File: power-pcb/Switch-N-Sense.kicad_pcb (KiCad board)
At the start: 2 copper layers, 94 x 57.5 mm, 44 parts, among them P1 CONN_01X01, P2 CONN_01X01, P3 CONN_01X01, P4 CONN_01X01, P5 CONN_01X01, P6 Conn_Switch-N-Sense, Q1 CSD18540Q5B, Q2 CSD18540Q5B, Q3 CSD18540Q5B, Q4 CSD18540Q5B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

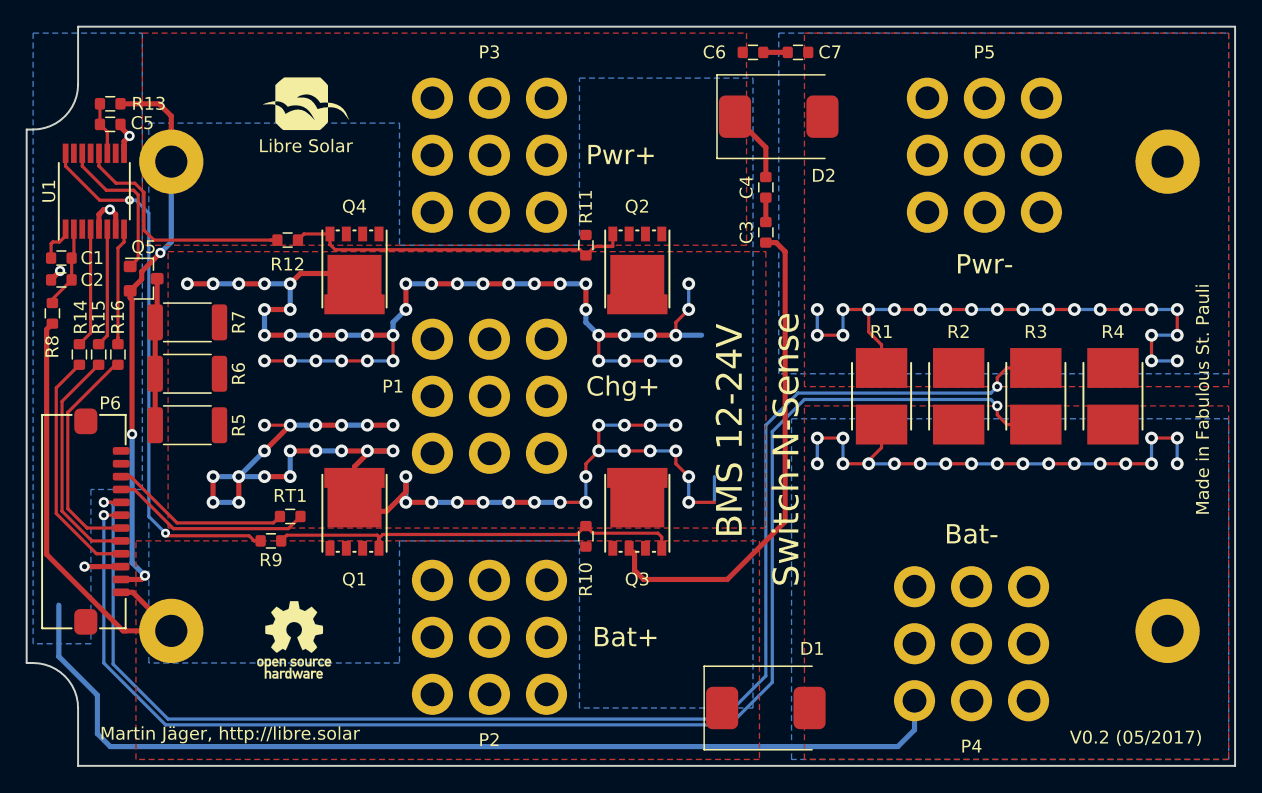
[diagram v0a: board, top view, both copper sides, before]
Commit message: Issues #1, #2 and #4 fixed
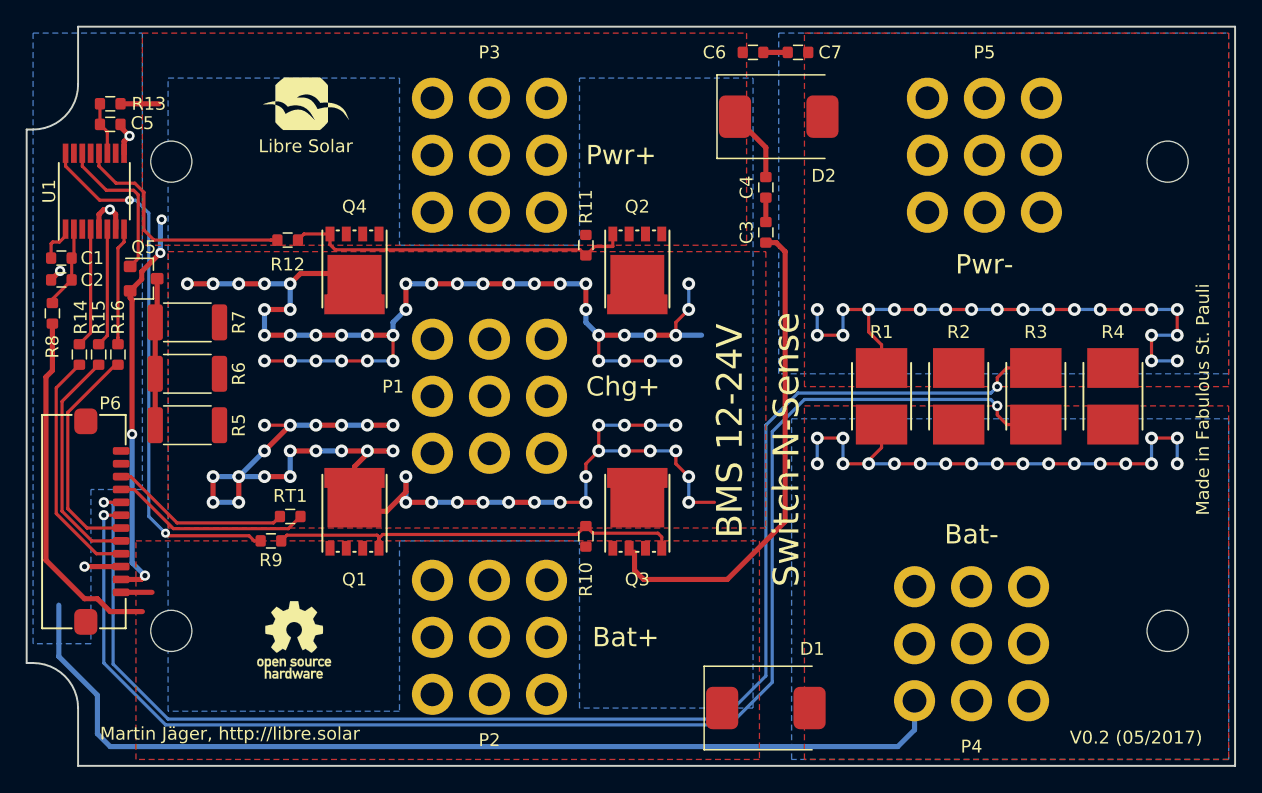
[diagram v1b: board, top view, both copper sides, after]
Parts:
- removed the REF** at (185.2, 70.5)
- removed the REF** at (185.2, 107.0)
- removed the REF** at (107.8, 107.0)
- removed the REF** at (107.8, 70.5)
- added REF**: MountingHole_3.2mm_M3, Mounting_Holes:MountingHole_3.2mm_M3, F.Cu at (107.8, 107.0)
- added REF**: MountingHole_3.2mm_M3, Mounting_Holes:MountingHole_3.2mm_M3, F.Cu at (107.8, 70.5)
- added REF**: MountingHole_3.2mm_M3, Mounting_Holes:MountingHole_3.2mm_M3, F.Cu at (185.2, 107.0)
- added REF**: MountingHole_3.2mm_M3, Mounting_Holes:MountingHole_3.2mm_M3, F.Cu at (185.2, 70.5)
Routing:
- net /LOAD+: track 49.6 -> 39.9 mm, vias 3 -> 4
- net /BAT+: track 73.5 -> 68.2 mm
- net (no net): track 2.00 -> 0.00 mm

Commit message: Issue #6 fixed
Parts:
- added R17: 1M, LibreSolar:R_0603_1608, F.Cu at (108.3, 79.5)
- D1, D2: value SMCJ36A -> SMCJ24A
- Q1, Q2, Q3, Q4: value CSD18540Q5B -> BSC010N04LS
- moved Q5 0.40 mm to (105.6, 79.2), turned to 90 degrees
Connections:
- Q5 pad 2: /LOAD+ -> Net-(Q5-Pad2)
- Q5 pad 3: Net-(Q5-Pad3) -> /LOAD+
- R5 pad 1: Net-(Q5-Pad3) -> Net-(Q5-Pad2)
- R6 pad 1: Net-(Q5-Pad3) -> Net-(Q5-Pad2)
- R7 pad 1: Net-(Q5-Pad3) -> Net-(Q5-Pad2)
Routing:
- net Net-(Q5-Pad2): track 0.00 -> 12.8 mm
- net Net-(Q5-Pad3): track 11.5 -> 0.00 mm
- net /PCHG_G: track 12.1 -> 17.7 mm
- net /CHG+: track 173.6 -> 171.6 mm, vias 77 -> 76
